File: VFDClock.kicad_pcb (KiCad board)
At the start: 2 copper layers, 76.2 x 53.3 mm, 22 parts, among them J1 Barrel_Jack_MountingPin, P1 Power, P2 Analog, P3 Digital, P4 Digital, Q1 VFD_LD8035E, Q2 VFD_LD8035E, Q3 VFD_LD8035E, Q4 VFD_LD8035E, Q5 VFD_LD8035E, Q6 VFD_LD8035E, U1 IC_HT16K33, U2 RTC_DS3231

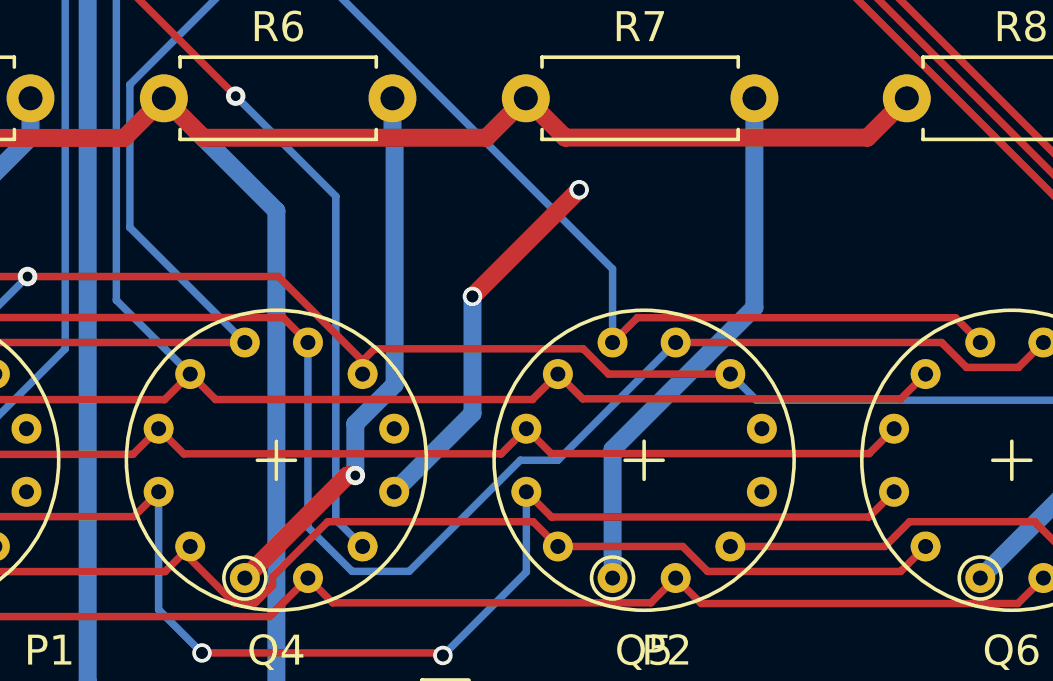
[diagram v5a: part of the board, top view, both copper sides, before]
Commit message: 綺麗じゃない線を修正
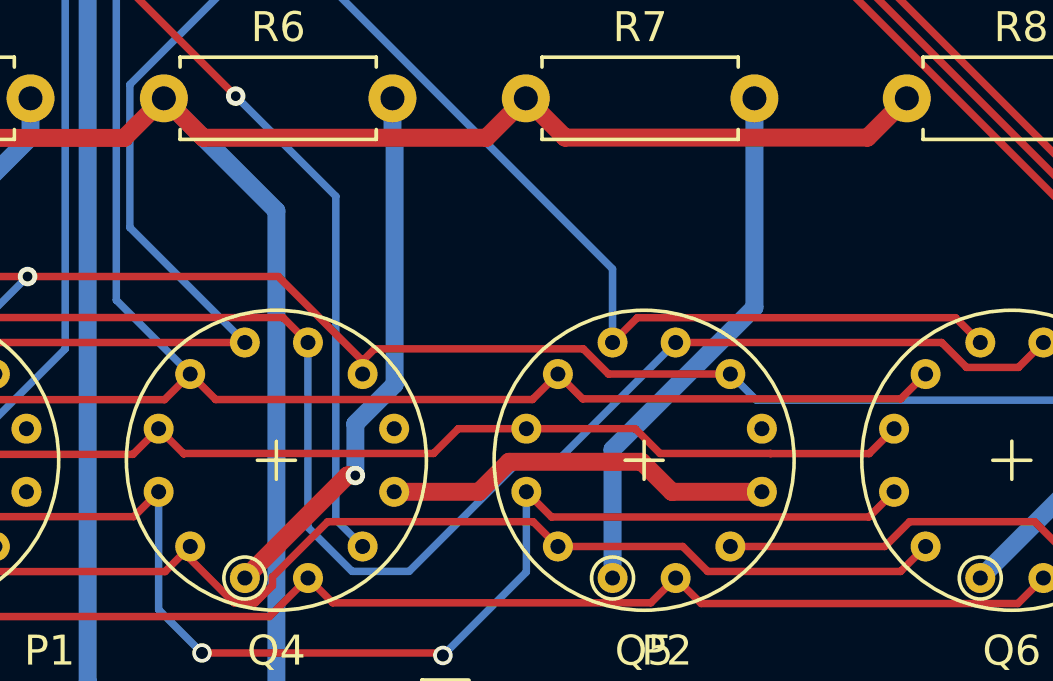
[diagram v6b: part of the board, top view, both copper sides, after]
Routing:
- net GND: track 47.5 -> 47.9 mm, vias 4 -> 2
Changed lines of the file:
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@@
     (thickness 1.6)
     (drawings 11)
-    (tracks 382)
+    (tracks 385)
     (zones 0)
     (modules 22)
@@
   (segment (start 136.525 98.323) (end 136.525 98.323) (width 0.6) (layer F.Cu) (net 2))
   (via (at 136.525 98.323) (size 0.65) (drill 0.4) (layers F.Cu B.Cu) (net 2))
-  (segment (start 159.314523 115.986841) (end 161.925 113.376364) (width 0.6) (layer B.Cu) (net 2))
-  (segment (start 161.925 113.376364) (end 161.925 109.474) (width 0.6) (layer B.Cu) (net 2))
-  (segment (start 161.925 109.474) (end 161.925 109.474) (width 0.6) (layer B.Cu) (net 2))
-  (via (at 161.925 109.474) (size 0.65) (drill 0.4) (layers F.Cu B.Cu) (net 2))
-  (segment (start 161.925 109.474) (end 165.481 105.918) (width 0.6) (layer F.Cu) (net 2))
-  (segment (start 165.481 105.918) (end 165.481 105.918) (width 0.6) (layer F.Cu) (net 2))
-  (via (at 165.481 105.918) (size 0.65) (drill 0.4) (layers F.Cu B.Cu) (net 2))
+  (segment (start 167.569943 114.98684) (end 168.569944 115.986841) (width 0.6) (layer F.Cu) (net 2))
+  (segment (start 168.569944 115.986841) (end 171.571523 115.986841) (width 0.6) (layer F.Cu) (net 2))
+  (segment (start 163.14316 114.98684) (end 167.569943 114.98684) (width 0.6) (layer F.Cu) (net 2))
+  (segment (start 162.143159 115.986841) (end 163.14316 114.98684) (width 0.6) (layer F.Cu) (net 2))
+  (segment (start 159.314523 115.986841) (end 162.143159 115.986841) (width 0.6) (layer F.Cu) (net 2))
   (segment (start 133.858 84.455) (end 133.858 83.3297) (width 0.25) (layer B.Cu) (net 3))
   (segment (start 132.334 75.565) (end 132.334 81.8057) (width 0.25) (layer B.Cu) (net 3))
@@
   (segment (start 152.908 121.3583) (end 160.8553 121.3583) (width 0.25) (layer F.Cu) (net 6))
   (segment (start 151.4635 113.8832) (end 152.3005 114.7202) (width 0.25) (layer F.Cu) (net 7))
-  (segment (start 152.3005 114.7202) (end 162.8835 114.7202) (width 0.25) (layer F.Cu) (net 7))
-  (segment (start 162.8835 114.7202) (end 163.7205 113.8832) (width 0.25) (layer F.Cu) (net 7))
   (segment (start 139.2065 114.7378) (end 150.6089 114.7378) (width 0.25) (layer F.Cu) (net 7))
   (segment (start 150.6089 114.7378) (end 151.4635 113.8832) (width 0.25) (layer F.Cu) (net 7))
@@
   (segment (start 117.7534 110.1452) (end 116.4558 110.1452) (width 0.25) (layer F.Cu) (net 7))
   (segment (start 116.4558 110.1452) (end 114.6925 111.9085) (width 0.25) (layer F.Cu) (net 7))
-  (segment (start 163.7205 113.8832) (end 164.5503 114.713) (width 0.25) (layer F.Cu) (net 7))
-  (segment (start 164.5503 114.713) (end 175.1477 114.713) (width 0.25) (layer F.Cu) (net 7))
   (segment (start 175.1477 114.713) (end 175.9775 113.8832) (width 0.25) (layer F.Cu) (net 7))
   (segment (start 114.6925 113.8832) (end 117.6215 116.8122) (width 0.25) (layer F.Cu) (net 7))
@@
   (segment (start 114.6925 113.883136) (end 114.692477 113.883159) (width 0.25) (layer B.Cu) (net 7))
   (segment (start 114.6925 111.9085) (end 114.6925 113.883136) (width 0.25) (layer B.Cu) (net 7))
+  (segment (start 171.85816 114.70816) (end 168.17516 114.70816) (width 0.25) (layer F.Cu) (net 7))
+  (segment (start 175.1477 114.713) (end 171.863 114.713) (width 0.25) (layer F.Cu) (net 7))
+  (segment (start 171.863 114.713) (end 171.85816 114.70816) (width 0.25) (layer F.Cu) (net 7))
+  (segment (start 167.350159 113.883159) (end 163.720477 113.883159) (width 0.25) (layer F.Cu) (net 7))
+  (segment (start 168.17516 114.70816) (end 167.350159 113.883159) (width 0.25) (layer F.Cu) (net 7))
+  (segment (start 163.720477 113.883159) (end 161.452841 113.883159) (width 0.25) (layer F.Cu) (net 7))
+  (segment (start 152.31254 114.70816) (end 152.3005 114.7202) (width 0.25) (layer F.Cu) (net 7))
+  (segment (start 160.62784 114.70816) (end 152.31254 114.70816) (width 0.25) (layer F.Cu) (net 7))
+  (segment (start 161.452841 113.883159) (end 160.62784 114.70816) (width 0.25) (layer F.Cu) (net 7))
   (segment (start 152.5153 112.0613) (end 151.6617 112.9149) (width 0.25) (layer F.Cu) (net 8))
   (segment (start 151.6617 112.9149) (end 141.1119 112.9149) (width 0.25) (layer F.Cu) (net 8))
@@
     (polygon
       (pts
-        (xy 162.941 116.586) (xy 158.115 116.586) (xy 158.877 115.189) (xy 162.941 115.189)
-      )
-    )
-  )
-  (zone (net 0) (net_name "") (layer F.Cu) (hatch edge 0.508)
-    (connect_pads (clearance 0.508))
-    (min_thickness 0.254)
-    (keepout (tracks allowed) (vias allowed) (copperpour not_allowed))
-    (fill (arc_segments 32) (thermal_gap 0.508) (thermal_bridge_width 0.508))
-    (polygon
-      (pts
-        (xy 174.879 116.459) (xy 170.815 116.459) (xy 171.069 115.062) (xy 175.514 115.062)
-      )
-    )
-  )
-  (zone (net 0) (net_name "") (layer F.Cu) (hatch edge 0.508)
-    (connect_pads (clearance 0.508))
-    (min_thickness 0.254)
-    (keepout (tracks allowed) (vias allowed) (copperpour not_allowed))
-    (fill (arc_segments 32) (thermal_gap 0.508) (thermal_bridge_width 0.508))
-    (polygon
-      (pts
         (xy 184.404 117.094) (xy 182.753 117.094) (xy 182.245 116.713) (xy 182.245 112.903) (xy 183.515 112.903)
       )
@@
       )
     )
+  )
+  (zone (net 0) (net_name "") (layer F.Cu) (hatch edge 0.508)
+    (connect_pads (clearance 0.508))
+    (min_thickness 0.254)
+    (keepout (tracks allowed) (vias allowed) (copperpour not_allowed))
+    (fill (arc_segments 32) (thermal_gap 0.508) (thermal_bridge_width 0.508))
+    (polygon
+      (pts
+        (xy 176.657 115.062) (xy 176.657 116.586) (xy 158.115 116.459) (xy 158.623 115.062) (xy 164.846 114.935)
+      )
+    )
